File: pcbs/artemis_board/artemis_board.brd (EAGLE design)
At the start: 96.5 x 71.1 mm, 277 parts, among them J1 10118192-0001LF, J2 FTSH-105-01-F-DV-007-K-P, Q10 BSS138K, Q11 2N7002K-7, Q12 BSS138K, Q13 2N7002K-7, Q14 BSS138K, Q15 2N7002K-7, Q16 BSS138K, Q17 2N7002K-7, Q18 BSS138K, Q19 2N7002K-7, Q20 BSS138K, Q21 2N7002K-7, Q22 BSS138K, Q23 2N7002K-7, Q24 BSS138K, Q25 2N7002K-7, Q26 BSS138K, Q27 2N7002K-7, Q28 BSS138K, Q29 2N7002K-7, Q30 BSS138K, Q31 2N7002K-7, Q32 BSS138K, Q33 2N7002K-7, Q34 BSS138K, Q35 2N7002K-7, Q36 BSS138K, Q5 2N7002K-7, Q6 BSS138K, Q7 2N7002K-7, Q8 BSS138K, Q9 2N7002K-7, U1 ARTEMIS_MODULESMD, U10 CDBHD140L-G, U11 CDBHD140L-G, U12 MAX9938, U13 TN2106K1-G, U14 CDBHD140L-G, U15 CDBHD140L-G, U16 CDBHD140L-G, U17 MAX9938, U18 TN2106K1-G, U19 CDBHD140L-G, U2 CP2102, U20 CDBHD140L-G, U21 74AXP1T45GWH, U22 TMUX1104DGSR, U23 CDBHD140L-G, U24 CDBHD140L-G, U25 MAX9938, U26 TN2106K1-G, U27 TMUX1104DGSR, U28 TMUX1104DGSR, U29 TPS62120, U3 74AXP1T45GWH, U30 TMUX1108RSVR, U31 CDBHD140L-G, U32 CDBHD140L-G, U33 CDBHD140L-G, U34 TMUX1108RSVR, U35 TMUX1108RSVR, U36 TMUX1108RSVR, U37 TMUX1104DGSR, U4 CDBHD140L-G, U5 CDBHD140L-G, U6 CDBHD140L-G, U7 CDBHD140L-G, U8 MAX9938, U9 TN2106K1-G

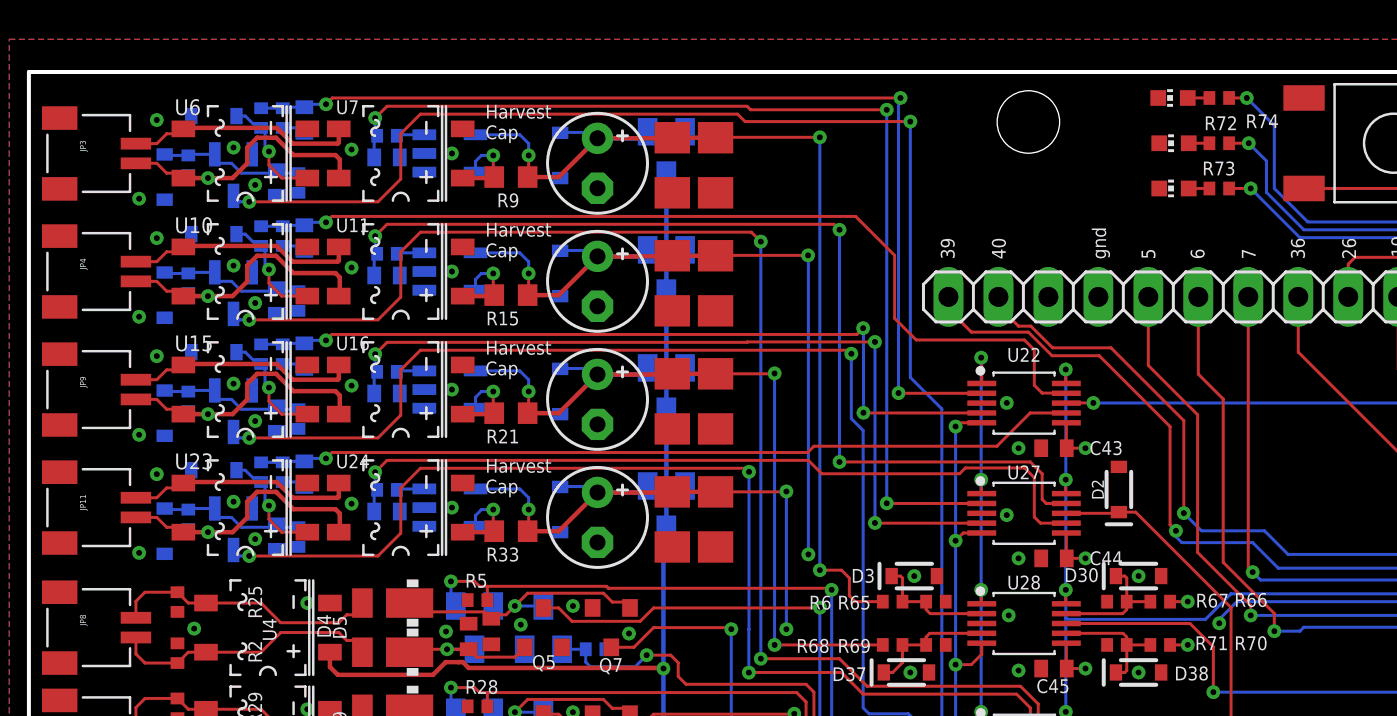
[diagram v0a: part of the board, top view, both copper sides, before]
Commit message: artemis energy harvesting board ready for ordering
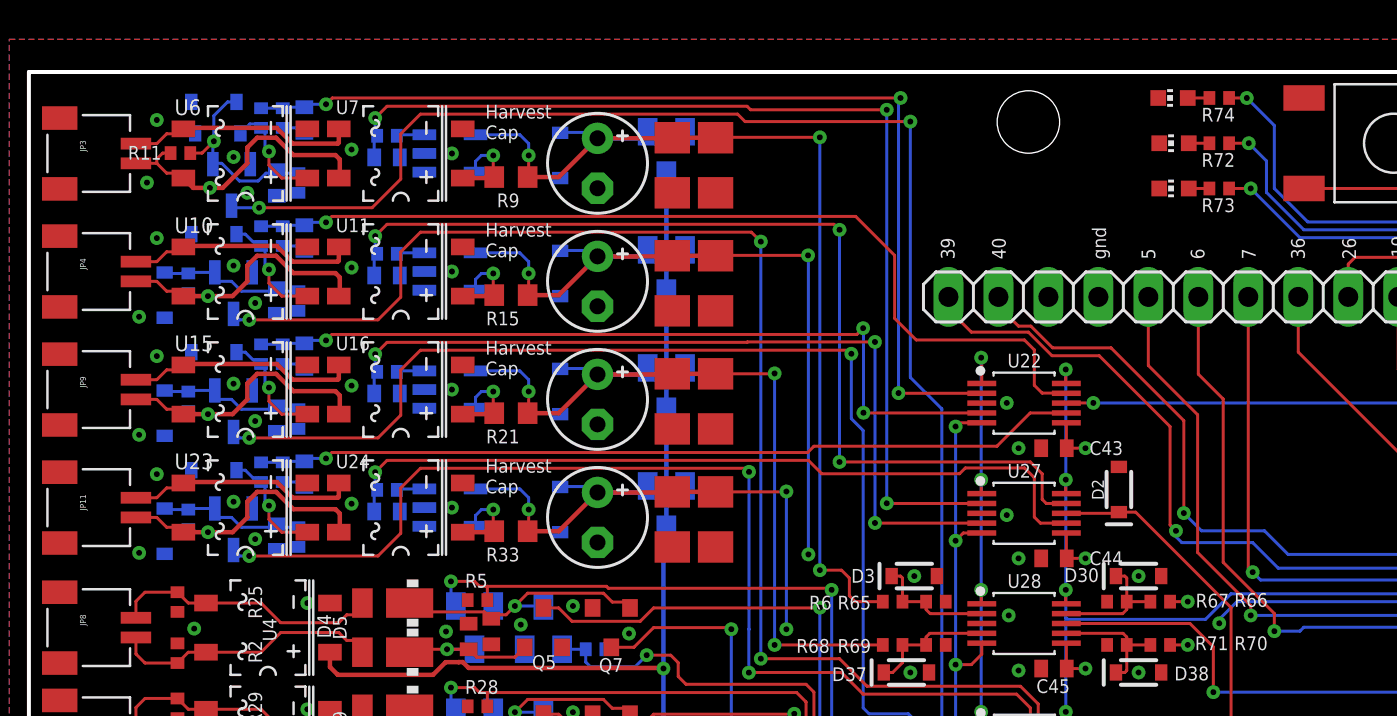
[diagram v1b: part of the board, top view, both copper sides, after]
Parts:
- moved D8 4.57 mm to (9.40, 69.6), turned to 0 degrees
- moved D9 0.90 mm to (9.60, 68.0)
- moved R11 0.74 mm to (7.70, 67.0), flipped to the top, turned to 180 degrees
- moved U9 0.51 mm to (10.3, 65.4)
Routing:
- net N$13: track 7.54 -> 10.5 mm, vias 0 -> 1
